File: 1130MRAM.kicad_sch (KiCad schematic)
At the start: 123 parts, among them J1 Screw_Terminal_01x02, J1A09 SLTpad, J1A11 SLTpad, K1E09 SLTpad, K1E11 SLTpad, M1A09 SLTpad, M1A11 SLTpad, M1C09 SLTpad, M1D09 SLTpad, M1E09 SLTpad, M1E11 SLTpad, SW1 SLTpad, U1 MR0A16AYS35, U10 74LS09, U11 74LS09, U12 SN74LVC1G123DCUR, U13 SN74LVC1G123DCUR, U14 74LS00, U2 SN74LVC244APWR, U3 SN74LVC244APWR, U4 LT8642S, U5 SN74LVC1G123DCUR, U6 SN74LVC1G123DCUR, U7 74LS09, U8 74LS09, U9 74LS09

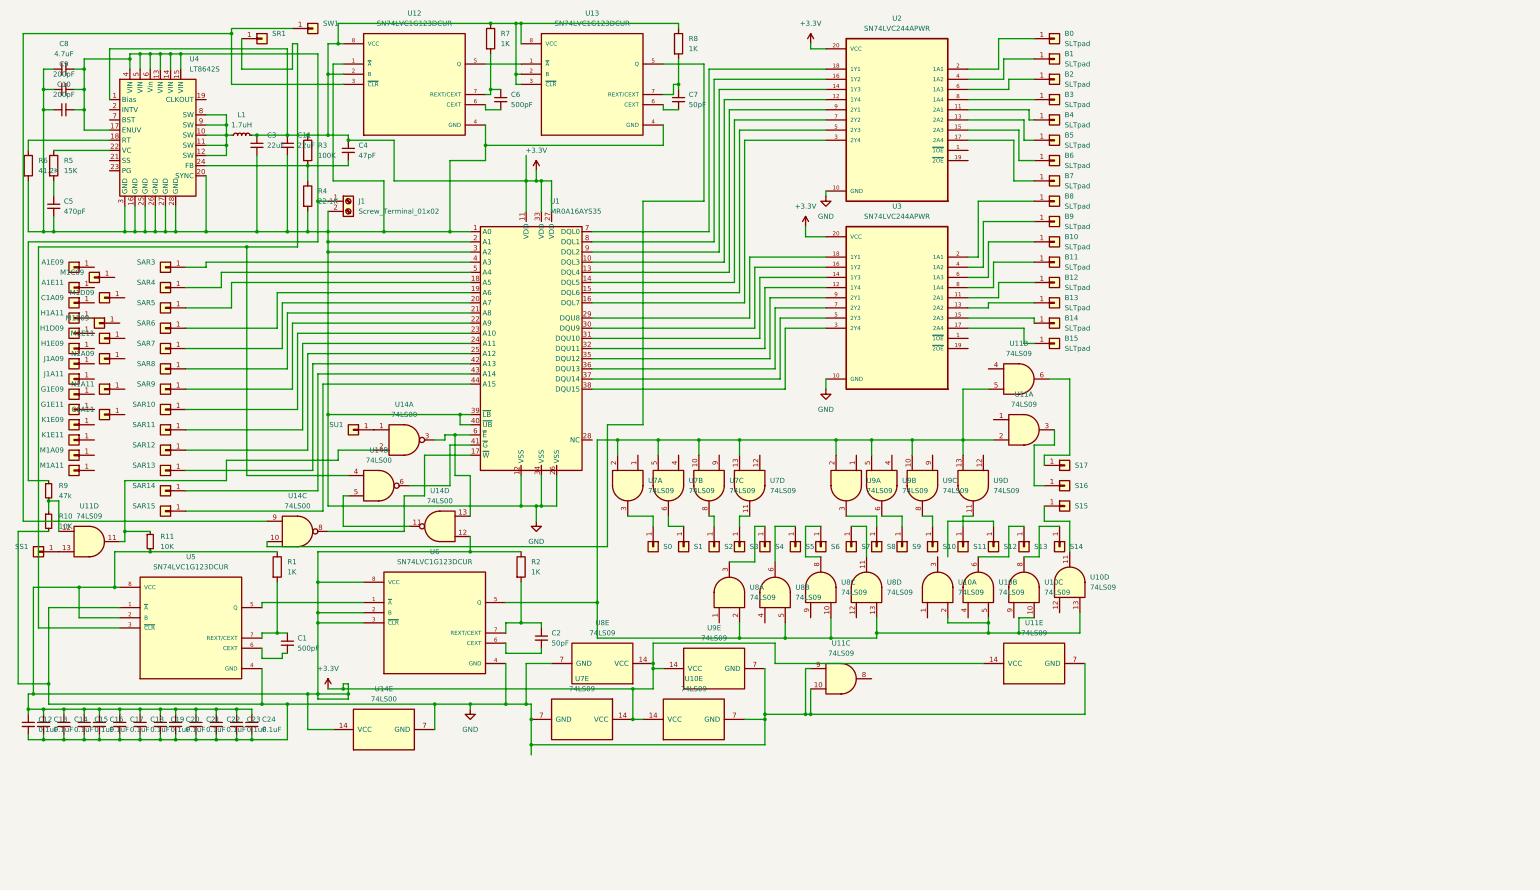
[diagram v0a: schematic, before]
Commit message: Completed design V1
prior to verification
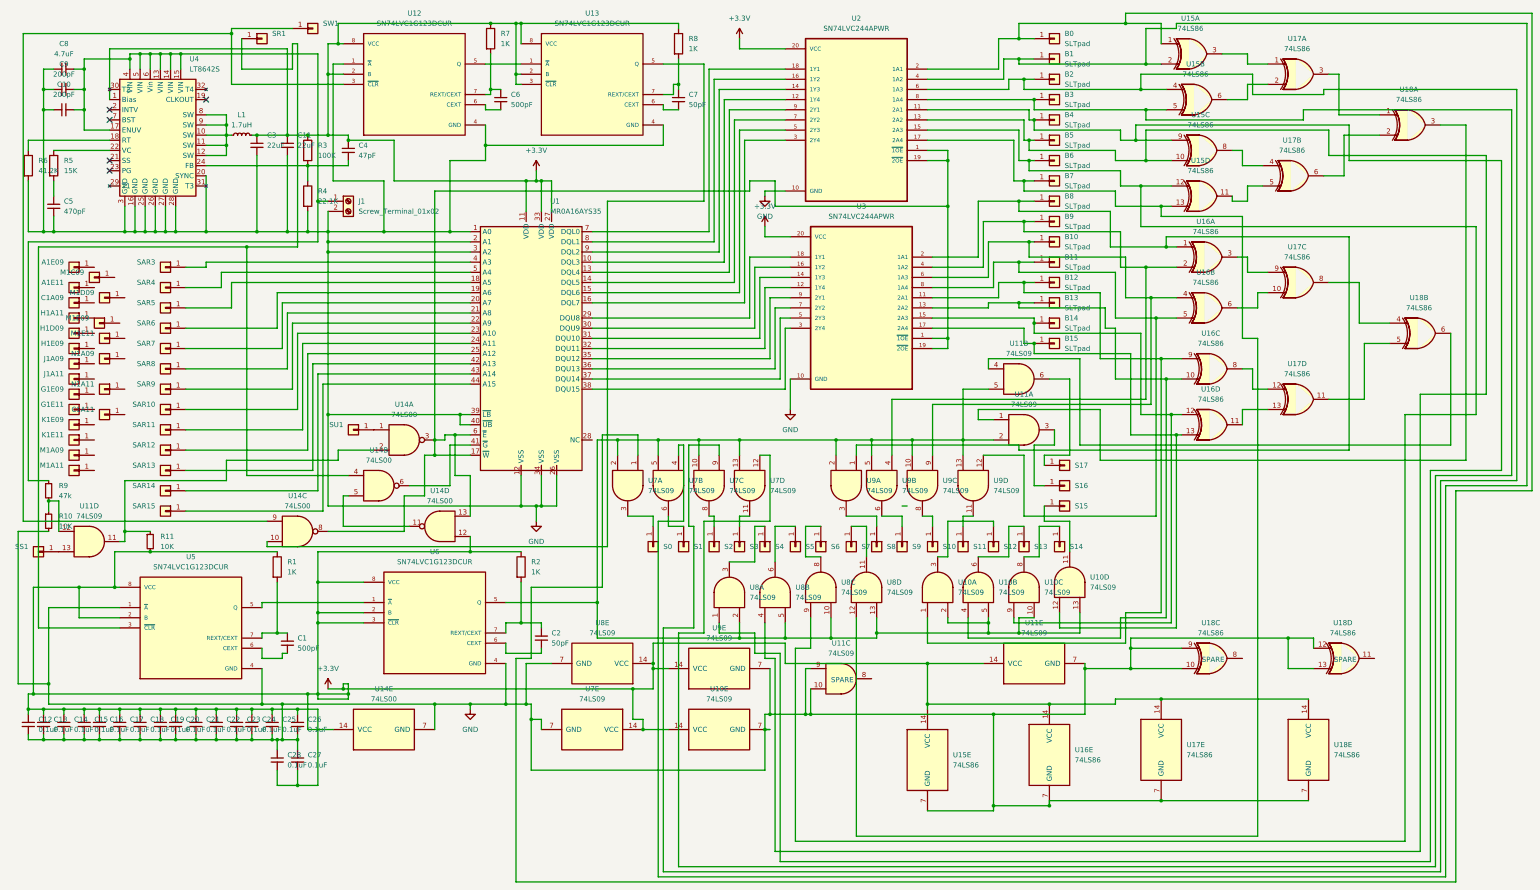
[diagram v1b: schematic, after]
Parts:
- added C25, C26, C27, C28: 0.1uF, Capacitor_SMD:C_0603_1608Metric, symbol Device:C_Small
- added U15, U16, U17, U18: 74LS86, Package_SO:TSSOP-14_4.4x5mm_P0.65mm, symbol carl:74HC86
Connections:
- net +3.3V: now also C25.1, C26.1, C27.2, C28.2, U15.14 (VCC), U16.14 (VCC), U17.14 (VCC), U18.14 (VCC)
- net GND: now also C25.2, C26.2, C27.1, C28.1, U15.7 (GND), U16.7 (GND), U17.7 (GND), U18.10, U18.12, U18.13, U18.7 (GND), U18.9
- net at B10.1 (Pin_1), U3.6 (1A3): now also U9.9, U16.4
- net at U1.6 (~{E}), U14.13, U14.3: now also U1.17 (~{W}), U14.8, U2.1 (~{1OE}), U2.19 (~{2OE}), U3.1 (~{1OE}), U3.19 (~{2OE})
- net at B5.1 (Pin_1), U2.13 (2A2): now also U8.4, U15.10
- net at U10.4: now also B13.1 (Pin_1), U3.13 (2A2), U16.10
- net at B8.1 (Pin_1), U3.2 (1A1): now also U9.1, U16.1
- net at U9.4: now also B9.1 (Pin_1), U3.4 (1A2), U16.2
- net at U10.12: now also B15.1 (Pin_1), U3.17 (2A4), U16.13
- net at B7.1 (Pin_1), U2.17 (2A4): now also U8.12, U15.13
- net at U7.9: now also B2.1 (Pin_1), U2.6 (1A3), U15.4
- net at B3.1 (Pin_1), U2.8 (1A4): now also U7.12, U15.5
- net at U11.1: now also U18.3
- net at B6.1 (Pin_1), U2.15 (2A3): now also U8.9, U15.12
- net at B14.1 (Pin_1), U3.15 (2A3): now also U10.9, U16.12
- net at B4.1 (Pin_1), U2.11 (2A1): now also U8.1, U15.9
- net at B12.1 (Pin_1), U3.11 (2A1): now also U10.1, U16.9
- net at B11.1 (Pin_1), U3.8 (1A4): now also U9.12, U16.5
- net at U10.3: now also S12.1 (Pin_1)
- net at U7.1: now also B0.1 (Pin_1), U2.2 (1A1), U15.1
- net at B1.1 (Pin_1), U2.4 (1A2): now also U7.4, U15.2
- net at U11.4: now also U18.6
- new net: U17.11, U18.5
- new net: U16.8, U17.12
- new net: U16.11, U17.13
- new net: U15.8, U17.4
- new net: U15.11, U17.5
- new net: U17.6, U18.2
- new net: U16.6, U17.10
- new net: U15.6, U17.2
- new net: U16.3, U17.9
- new net: U17.3, U18.1
- new net: U17.8, U18.4
- new net: U15.3, U17.1
- no-connect marks 0 -> 5
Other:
- note added: "SPARE"
- moved on the sheet: U10E, U2, U3, U7E, U9E

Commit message: Latest version with fixes
fixed parity circuits, went to 4 layer board
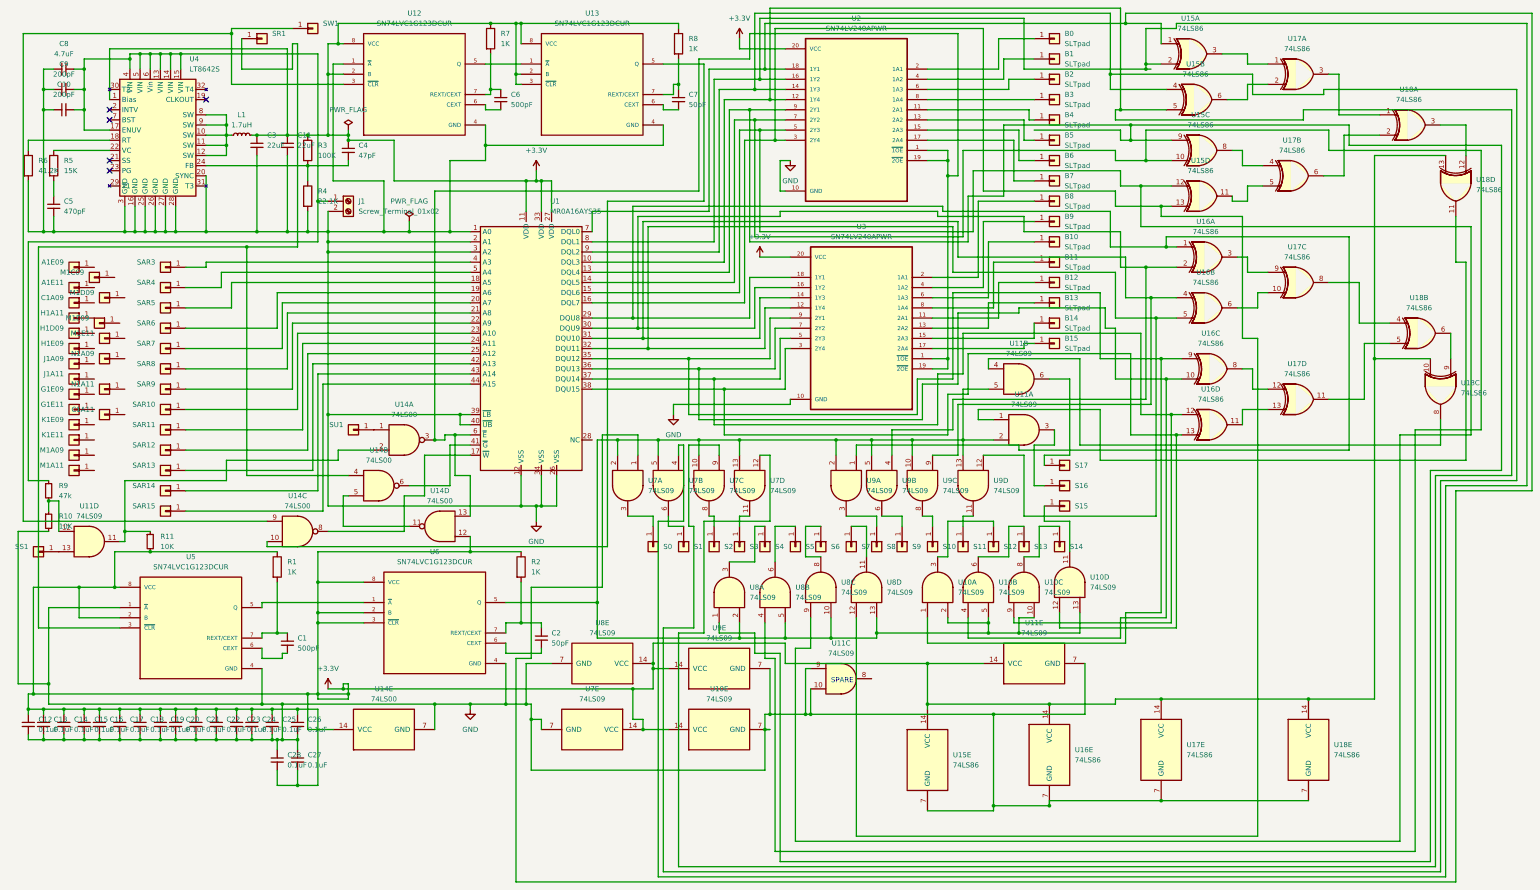
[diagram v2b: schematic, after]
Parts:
- U2, U3: value SN74LVC244APWR -> SN74LV240APWR; symbol carl:SN74LVC244APWR -> carl:SN74LV240APWR
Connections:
- net +3.3V: now also U18.10, U18.13
- net GND: no longer U18.10, U18.12, U18.13, U18.9
- net at B10.1 (Pin_1), U3.6 (1A3): no longer U16.4, U9.9
- net at U1.6 (~{E}), U14.13, U14.3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: no longer U1.17 (~{W}), U14.8
- net at B5.1 (Pin_1), U2.13 (2A2): no longer U15.10, U8.4
- net at U10.4, U16.10: now also U1.36 (DQU13), U3.7 (2Y2); no longer B13.1 (Pin_1), U3.13 (2A2)
- net at B8.1 (Pin_1), U3.2 (1A1): no longer U16.1, U9.1
- net at U18.8: now also U11.4
- net at U18.11: now also U11.1
- net at U16.2, U9.4: now also U1.30 (DQU9), U3.16 (1Y2); no longer B9.1 (Pin_1), U3.4 (1A2)
- net at U10.12, U16.13: now also U1.38 (DQU15), U3.3 (2Y4); no longer B15.1 (Pin_1), U3.17 (2A4)
- net at U16.5, U9.12: now also U1.32 (DQU11), U3.12 (1Y4); no longer B11.1 (Pin_1), U3.8 (1A4)
- net at U15.4, U7.9: now also U1.9 (DQL2), U2.14 (1Y3); no longer B2.1 (Pin_1), U2.6 (1A3)
- net at U15.5, U7.12: now also U1.10 (DQL3), U2.12 (1Y4); no longer B3.1 (Pin_1), U2.8 (1A4)
- net at U15.9, U8.1: now also U1.13 (DQL4), U2.9 (2Y1); no longer B4.1 (Pin_1), U2.11 (2A1)
- net at U10.9, U16.12: now also U1.37 (DQU14), U3.5 (2Y3); no longer B14.1 (Pin_1), U3.15 (2A3)
- net at B7.1 (Pin_1), U2.17 (2A4): no longer U15.13, U8.12
- net at U18.3: now also U18.12; no longer U11.1
- net at B6.1 (Pin_1), U2.15 (2A3): no longer U15.12, U8.9
- net at U10.1, U16.9: now also U1.35 (DQU12), U3.9 (2Y1); no longer B12.1 (Pin_1), U3.11 (2A1)
- net at U15.1, U7.1: now also U1.7 (DQL0), U2.18 (1Y1); no longer B0.1 (Pin_1), U2.2 (1A1)
- net at U1.8 (DQL1), U2.16 (1Y2): now also U15.2, U7.4
- net at U1.16 (DQL7), U2.3 (2Y4): now also U15.13, U8.12
- net at B1.1 (Pin_1), U2.4 (1A2): no longer U15.2, U7.4
- net at U1.15 (DQL6), U2.5 (2Y3): now also U15.12, U8.9
- net at U1.14 (DQL5), U2.7 (2Y2): now also U15.10, U8.4
- net at U1.29 (DQU8), U3.18 (1Y1): now also U16.1, U9.1
- net at U1.31 (DQU10), U3.14 (1Y3): now also U16.4, U9.9
- net at U18.6: now also U18.9; no longer U11.4
- new net: B3.1 (Pin_1), U2.8 (1A4)
- new net: B14.1 (Pin_1), U3.15 (2A3)
- new net: B4.1 (Pin_1), U2.11 (2A1)
- new net: B12.1 (Pin_1), U3.11 (2A1)
- new net: B11.1 (Pin_1), U3.8 (1A4)
- new net: B13.1 (Pin_1), U3.13 (2A2)
- new net: B2.1 (Pin_1), U2.6 (1A3)
- new net: B9.1 (Pin_1), U3.4 (1A2)
- new net: B0.1 (Pin_1), U2.2 (1A1)
- new net: U1.17 (~{W}), U14.8
- new net: B15.1 (Pin_1), U3.17 (2A4)
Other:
- moved on the sheet: U18C, U18D, U3

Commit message: Annotations and cleanup
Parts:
- C1: value 500pF -> 470pF
- C2, C7: value 50pF -> 47pF
- C6: value 500pF -> 470pF; now left out of the parts list
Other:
- note added: "(~P1)*RQ"
- note added: "(~P2)*RQ"
- note added: "+12V down to +3.3V"
- note added: "+SS*+12V"
- note added: "+SS*+12V*+SU"
- note added: "+Storage Read"
- note added: "+Storage Select"
- note added: "+Storage Use"
- note added: "+Storage Write"
- note added: "DQx*RQ"
- note added: "MRAM"
- note added: "Odd parity P1"
- note added: "Odd parity P2"
- note added: "Pass Bx to DQx"
- note added: "Q for 800 ns"
- note added: "Trigger +SR goes high"
- note added: "Trigger +SW goes high"
- note added: "Trigger U12 Q goes low"
- note added: "Trigger U5 Q goes low"
- note added: "~(+SS*+12V*+SU)"
- note added: "~(+SS*+12V*+SU*+SR)"
- note added: "~(+SW*WQ)"
- note added: "~(Odd parity P1)"
- note added: "~(Odd parity P2)"
- moved on the sheet: SR1, SW1

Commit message: Corrections to design
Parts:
- removed R11: 10K, Resistor_SMD:R_0805_2012Metric, symbol Device:R_Small
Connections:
- net GND: now also U11.12, U11.13
- net at U14.2: now also R10.1, R9.2; no longer U11.11
- net at U2.1 (~{1OE}), U2.19 (~{2OE}), U3.1 (~{1OE})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: now also U1.17 (~{W}), U14.8; no longer U1.6 (~{E}), U14.13, U14.3
- net at SS1.1 (Pin_1): no longer U11.13
- new net: U1.6 (~{E}), U14.13, U14.3
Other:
- note added: "+12V"
- note added: "+12V * +SU"
- note added: "~(+12V * +SU * +SR)"
- note added: "~(+12V * +SU)"
- note added: "~(+SW * WQ)"
- note removed: "+SS*+12V"
- note removed: "+SS*+12V*+SU"
- note removed: "~(+SS*+12V*+SU)"
- note removed: "~(+SS*+12V*+SU*+SR)"
- note removed: "~(+SW*WQ)"
- moved on the sheet: C1A11, M1C09, M1D09, SS1, U11D

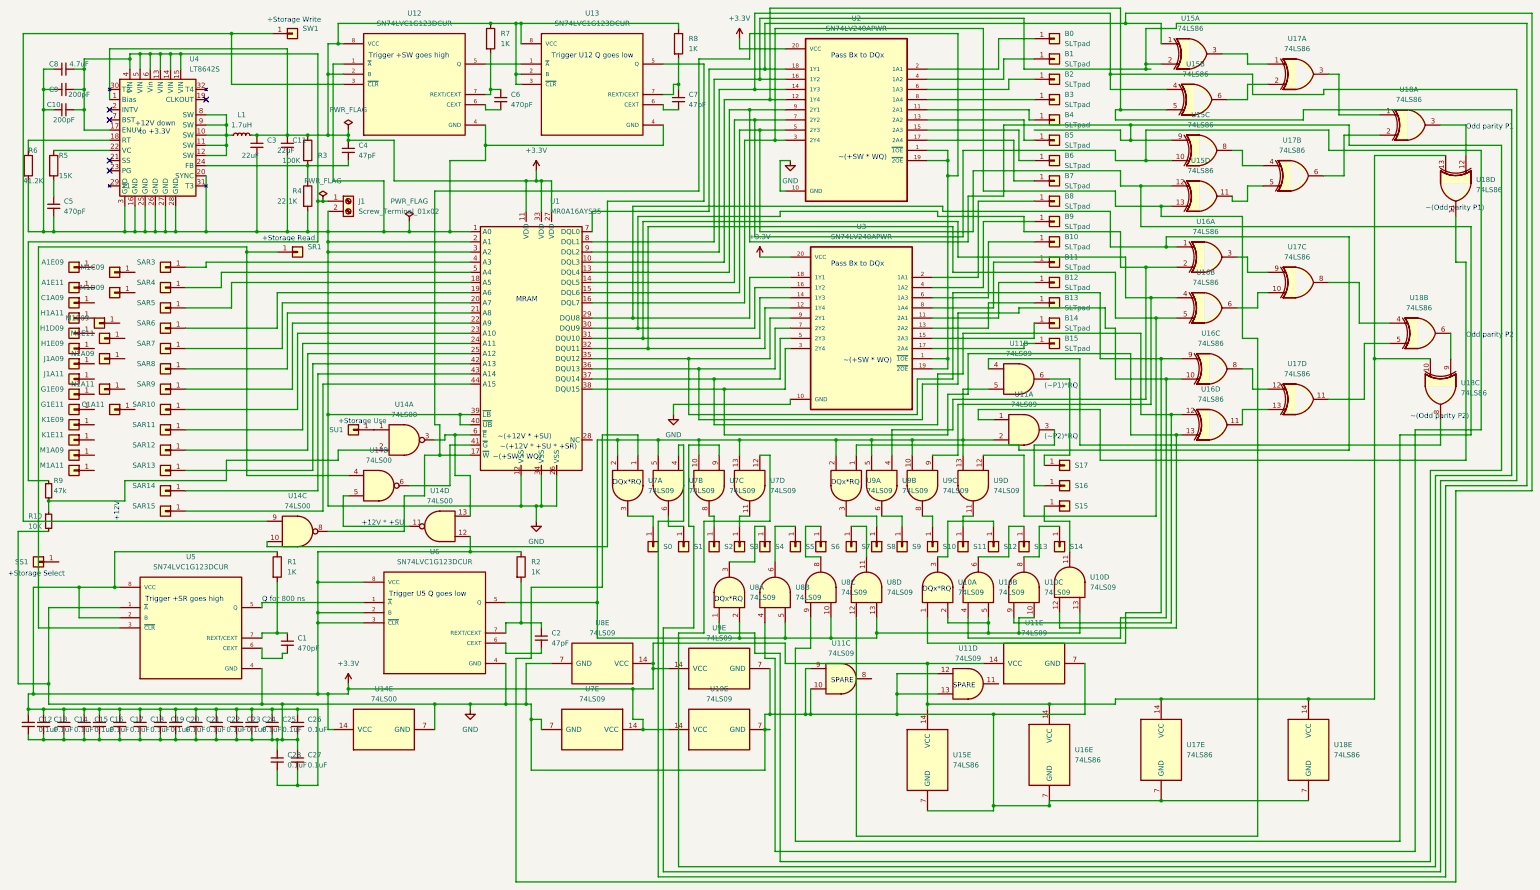
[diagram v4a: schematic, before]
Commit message: Debugged version of KiCAD files
Created project library for the symbols and footprints used with this design
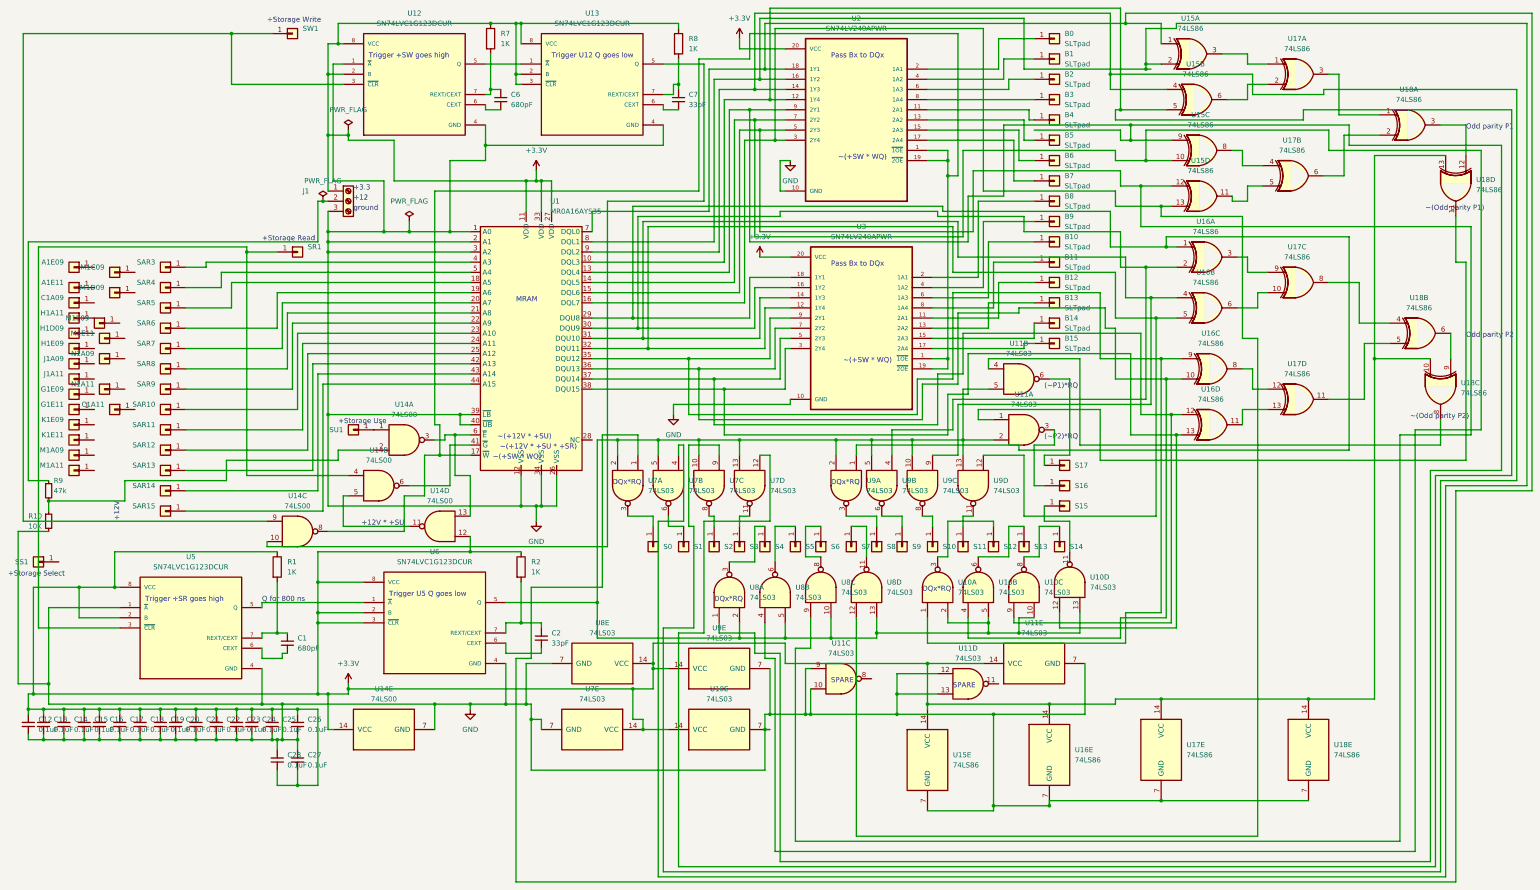
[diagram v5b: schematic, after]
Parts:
- removed C10, C9: 200pF, Capacitor_SMD:C_0603_1608Metric, symbol Device:C_Small
- removed C11, C3: 22uF, Capacitor_SMD:C_1210_3225Metric, symbol Device:C_Small
- removed C4: 47pF, Capacitor_SMD:C_0603_1608Metric, symbol Device:C_Small
- removed C5: 470pF, Capacitor_SMD:C_0603_1608Metric, symbol Device:C_Small
- removed C8: 4.7uF, Capacitor_SMD:C_0805_2012Metric, symbol Device:C_Small
- removed L1: 1.7uH, Inductor_SMD:L_Wuerth_WE-TPC-3816, symbol Device:L_Small
- removed R3: 100K, Resistor_SMD:R_0805_2012Metric, symbol Device:R
- removed R4: 22.1K, Resistor_SMD:R_0805_2012Metric, symbol Device:R
- removed R5: 15K, Resistor_SMD:R_0805_2012Metric, symbol Device:R
- removed R6: 41.2K, Resistor_SMD:R_0805_2012Metric, symbol Device:R
- removed U4: LT8642S, Library.carl:LT8642SEV, symbol carl:LT8642S
- A1E09, A1E11, B0, B1, B10, B11, B12, B13, B14, B15, B2, B3, B4, B5, B6, B7, B8, B9, C1A09, C1A11, G1E09, G1E11, H1A11, H1D09, H1E09, J1A09, J1A11, K1E09, K1E11, M1A09, M1A11, M1C09, M1D09, M1E09, M1E11, N1A09, N1A11, S0, S1, S10, S11, S12, S13, S14, S15, S16, S17, S2, S3, S4, S5, S6, S7, S8, S9, SAR10, SAR11, SAR12, SAR13, SAR14, SAR15, SAR3, SAR4, SAR5, SAR6, SAR7, SAR8, SAR9, SR1, SS1, SU1, SW1: footprint Library.carl:SLT -> 1130MRAM:SLT; symbol carl:SLTpad -> 1130mram:SLTpad
- C1, C6: value 470pF -> 680pF
- C2, C7: value 47pF -> 33pF
- J1: value Screw_Terminal_01x02 -> Screw_Terminal_01x03; footprint Library.carl:CONN2 screw -> Connector_Phoenix_MC_HighVoltage:PhoenixContact_MCV_1,5_3-G-5.08_1x03_P5.08mm_Vertical; symbol Connector:Screw_Terminal_01x02 -> Connector:Screw_Terminal_01x03
- U1: symbol carl:MR0A16A_MRAM -> 1130mram:MR0A16A_MRAM
- U10, U11, U7, U8, U9: value 74LS09 -> 74LS03; footprint Library.carl:sn74lc09dr -> 1130MRAM:sn74lc03dr; symbol carl:74LS09 -> 1130mram:74LS03
- U12, U13, U5, U6: footprint Library.carl:sn74lvc1g123dcur -> 1130MRAM:sn74lvc1g123dcur; symbol carl:SN74LVC1G123DCUR -> 1130mram:SN74LVC1G123DCUR
- U15, U16, U17, U18: symbol carl:74HC86 -> 1130mram:74HC86
- U2, U3: footprint Library.carl:sn74lvc244a -> 1130MRAM:sn74lvc244a; symbol carl:SN74LV240APWR -> 1130mram:SN74LV240APWR
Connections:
- net +3.3V: now also J1.1 (Pin_1)
- net GND: now also J1.3 (Pin_3); no longer J1.2 (Pin_2)
- net at R9.1: now also J1.2 (Pin_2); no longer J1.1 (Pin_1)
- no-connect marks 5 -> 0
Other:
- note added: "+12"
- note added: "+3.3"
- note added: "ground"
- note removed: "+12V down to +3.3V"
